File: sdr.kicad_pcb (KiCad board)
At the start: 4 copper layers, 65 x 56 mm, 224 parts, among them J1 RX, J2 TX, SW1 KMR231NGLFS, T1 B0322J5050, T2 B0322J5050, T3 TR_TC1-1-43X+, T4 TR_TC1-1-43X+, U1 FT601, U10 MIC94310, U11 PAM2305, U12 BGS12, U13 BGS12, U14 FT232HL, U15 93LCxxBT-I/OT, U3 LMS6002DR2, U4 ECP5, U5 Si5351, U6 PAM2305, U7 NCP186, U8 MIC94310, U9 MIC94310, X1 GSB443133HR, X2 JTAG, X3 RaspberryPiConnector, X4 JTAG, X5 USB_OTG, Y1 FL3000027, Y2 ABM11-141, Y3 ABLS2-12.000MHZ-D4Y-T

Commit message: Fix shield lines again.
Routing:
- net GNDD: track 839.6 -> 844.2 mm
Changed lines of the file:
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@@
 (kicad_pcb (version 4) (host pcbnew 4.0.6-e0-6349~53~ubuntu14.04.1)
   (general
-    (links 0)
+    (links 822)
     (no_connects 0)
-    (area 83.616521 95.152522 181.005759 157.677001)
+    (area 99.924999 99.924999 165.075001 156.075001)
     (thickness 1.6)
     (drawings 25)
-    (tracks 3914)
+    (tracks 3918)
     (zones 0)
     (modules 224)
@@
   )
   (setup
-    (last_trace_width 0.127)
+    (last_trace_width 0.762)
     (user_trace_width 0.2032)
     (user_trace_width 0.254)
@@
     (visible_elements FFFFFF79)
     (pcbplotparams
-      (layerselection 0x000fc_80000007)
-      (usegerberextensions false)
-      (excludeedgelayer false)
+      (layerselection 0x010fc_80000007)
+      (usegerberextensions true)
+      (excludeedgelayer true)
       (linewidth 0.100000)
       (plotframeref false)
@@
   (gr_line (start 158.1 106.4) (end 158.1 111.4) (angle 90) (layer F.CrtYd) (width 0.2))
   (segment (start 158.508601 127.108601) (end 158.3 126.9) (width 0.2032) (layer B.Cu) (net 0))
-  (segment (start 157.2709 135.4709) (end 157.47238 135.67238) (width 0.762) (layer B.Cu) (net 3))
-  (segment (start 157.47238 135.67238) (end 157.47238 137.5664) (width 0.762) (layer B.Cu) (net 3))
-  (segment (start 155.33116 135.4709) (end 157.2709 135.4709) (width 0.762) (layer B.Cu) (net 3))
+  (segment (start 157.47238 135.65886) (end 157.30982 135.4963) (width 0.762) (layer B.Cu) (net 3))
+  (segment (start 157.30982 135.4963) (end 155.7528 135.4963) (width 0.762) (layer B.Cu) (net 3))
+  (segment (start 157.47238 150.42262) (end 157.47238 135.65886) (width 0.762) (layer B.Cu) (net 3))
+  (segment (start 155.7528 135.4963) (end 149.0754 135.4963) (width 0.762) (layer F.Cu) (net 3))
+  (segment (start 149.0754 135.4963) (end 149.05 135.4709) (width 0.762) (layer F.Cu) (net 3))
+  (segment (start 157.46984 135.66648) (end 157.29966 135.4963) (width 0.762) (layer F.Cu) (net 3))
+  (segment (start 157.29966 135.4963) (end 155.7528 135.4963) (width 0.762) (layer F.Cu) (net 3))
+  (segment (start 157.46984 137.62736) (end 157.46984 135.66648) (width 0.762) (layer F.Cu) (net 3))
+  (segment (start 157.47238 140.48232) (end 157.47238 137.6299) (width 0.762) (layer F.Cu) (net 3))
+  (segment (start 157.47238 137.6299) (end 157.46984 137.62736) (width 0.762) (layer F.Cu) (net 3))
+  (via (at 155.7528 135.4963) (size 0.6858) (drill 0.381) (layers F.Cu B.Cu) (net 3))
+  (via (at 157.46984 137.62736) (size 0.6858) (drill 0.381) (layers F.Cu B.Cu) (net 3))
+  (segment (start 149.05 135.4709) (end 142.24762 135.4709) (width 0.762) (layer F.Cu) (net 3))
+  (segment (start 148.14296 135.4709) (end 147.5613 134.88924) (width 0.762) (layer B.Cu) (net 3))
   (segment (start 107.67568 130.83654) (end 103.26764 130.83654) (width 0.762) (layer F.Cu) (net 3))
   (segment (start 103.26764 130.83654) (end 102.5525 131.55168) (width 0.762) (layer F.Cu) (net 3))
@@
   (segment (start 150.41372 134.72444) (end 149.66726 135.4709) (width 0.254) (layer B.Cu) (net 3))
   (segment (start 149.66726 135.4709) (end 149.05 135.4709) (width 0.254) (layer B.Cu) (net 3))
-  (segment (start 147.96262 135.4709) (end 149.05 135.4709) (width 0.762) (layer F.Cu) (net 3))
-  (segment (start 149.05 135.4709) (end 155.33116 135.4709) (width 0.762) (layer F.Cu) (net 3))
   (segment (start 147.33548 134.08246) (end 148.72392 135.4709) (width 0.254) (layer B.Cu) (net 3))
   (segment (start 148.72392 135.4709) (end 149.05 135.4709) (width 0.254) (layer B.Cu) (net 3))
   (via (at 149.05 135.4709) (size 0.6858) (drill 0.381) (layers F.Cu B.Cu) (net 3))
-  (segment (start 147.96262 135.4709) (end 142.24762 135.4709) (width 0.762) (layer F.Cu) (net 3))
   (segment (start 147.98548 133.32846) (end 148.89866 133.32846) (width 0.254) (layer B.Cu) (net 3))
   (segment (start 148.89866 133.32846) (end 149.12086 133.55066) (width 0.254) (layer B.Cu) (net 3))
@@
   (segment (start 155.93 129.77682) (end 155.32608 130.38074) (width 0.127) (layer B.Cu) (net 3))
   (via (at 155.32608 130.38074) (size 0.6858) (drill 0.381) (layers F.Cu B.Cu) (net 3))
-  (segment (start 157.47238 150.42262) (end 157.47238 137.5664) (width 0.762) (layer B.Cu) (net 3))
   (segment (start 156.5529 153.9541) (end 156.5529 151.3421) (width 0.762) (layer B.Cu) (net 3))
   (segment (start 156.5529 151.3421) (end 157.47238 150.42262) (width 0.762) (layer B.Cu) (net 3))
-  (via (at 155.33116 135.4709) (size 0.6858) (drill 0.381) (layers F.Cu B.Cu) (net 3))
   (segment (start 157.47238 146.04238) (end 157.47238 150.42262) (width 0.762) (layer F.Cu) (net 3))
   (via (at 157.47238 150.42262) (size 0.6858) (drill 0.381) (layers F.Cu B.Cu) (net 3))
@@
   (via (at 157.47238 143.40078) (size 0.6858) (drill 0.381) (layers F.Cu B.Cu) (net 3))
   (via (at 157.47238 140.48232) (size 0.6858) (drill 0.381) (layers F.Cu B.Cu) (net 3))
-  (segment (start 157.47238 137.5664) (end 157.47238 140.48232) (width 0.762) (layer F.Cu) (net 3))
-  (via (at 157.47238 137.5664) (size 0.6858) (drill 0.381) (layers F.Cu B.Cu) (net 3))
   (segment (start 156.5529 153.9541) (end 156.5529 151.3421) (width 0.762) (layer F.Cu) (net 3))
   (segment (start 156.5529 151.3421) (end 157.47238 150.42262) (width 0.762) (layer F.Cu) (net 3))

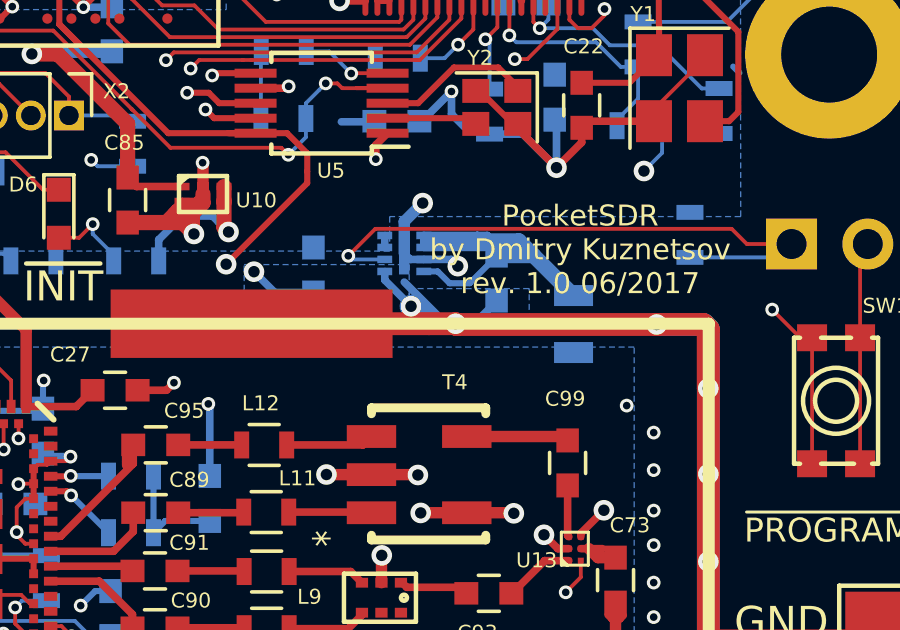
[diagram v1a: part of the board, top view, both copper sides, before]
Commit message: Start fixing problems with mask size and copper zone clearance.
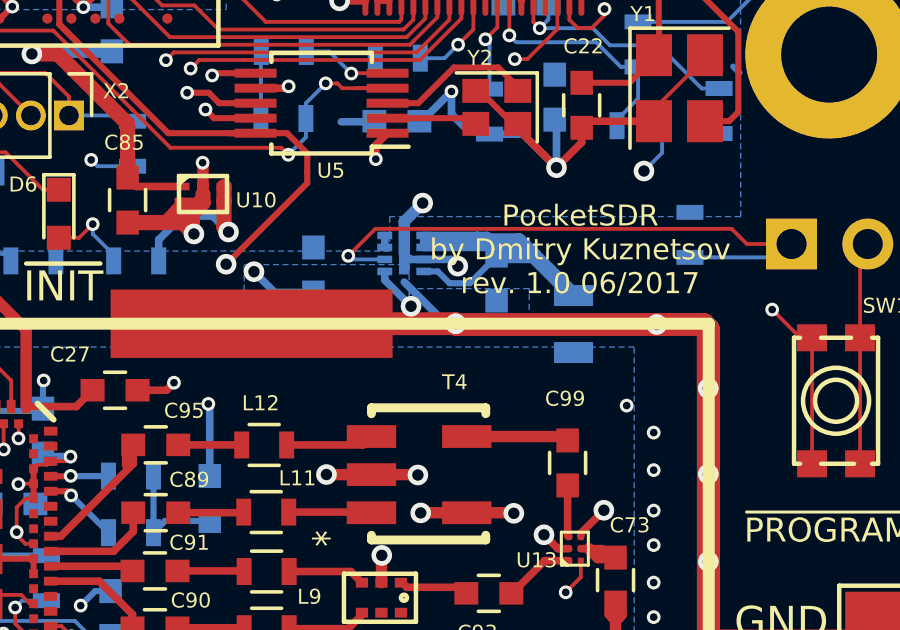
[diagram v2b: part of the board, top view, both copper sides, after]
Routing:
- net GNDD: track 844.2 -> 842.3 mm
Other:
- rule pad_to_mask_clearance: 0.2 -> 0.07112
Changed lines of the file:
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@@
-(kicad_pcb (version 4) (host pcbnew 4.0.6-e0-6349~53~ubuntu14.04.1)
+(kicad_pcb (version 4) (host pcbnew 4.0.7-e0-6372~58~ubuntu16.04.1)
   (general
     (links 822)
-    (no_connects 0)
-    (area 99.924999 99.924999 165.075001 156.075001)
+    (no_connects 6)
+    (area 83.616521 95.152522 181.005759 157.677001)
     (thickness 1.6)
     (drawings 25)
-    (tracks 3918)
+    (tracks 3916)
     (zones 0)
     (modules 224)
@@
   (title_block
     (title PocketSDR)
-    (date 2017-06-19)
-    (rev 1.0)
+    (date 2017-07-21)
+    (rev 1.1)
   )
   (layers
-    (0 F.Cu signal)
+    (0 F.Cu signal hide)
     (1 In1.Cu power hide)
-    (2 In2.Cu signal)
+    (2 In2.Cu signal hide)
     (31 B.Cu signal)
     (32 B.Adhes user hide)
@@
     (35 F.Paste user hide)
     (36 B.SilkS user)
-    (37 F.SilkS user)
-    (38 B.Mask user hide)
+    (37 F.SilkS user hide)
+    (38 B.Mask user)
     (39 F.Mask user hide)
     (40 Dwgs.User user hide)
@@
   )
   (setup
-    (last_trace_width 0.762)
+    (last_trace_width 0.127)
     (user_trace_width 0.2032)
     (user_trace_width 0.254)
@@
     (user_trace_width 0.762)
     (trace_clearance 0.127)
-    (zone_clearance 0.127)
+    (zone_clearance 0.254)
     (zone_45_only no)
     (trace_min 0.127)
@@
     (pad_size 0.29718 0.29718)
     (pad_drill 0)
-    (pad_to_mask_clearance 0.2)
+    (pad_to_mask_clearance 0.07112)
+    (solder_mask_min_width 0.127)
     (aux_axis_origin 124.58 122.04)
     (visible_elements FFFFFF79)
     (pcbplotparams
-      (layerselection 0x010fc_80000007)
-      (usegerberextensions true)
-      (excludeedgelayer true)
+      (layerselection 0x01010_00000000)
+      (usegerberextensions false)
+      (excludeedgelayer false)
       (linewidth 0.100000)
       (plotframeref false)
@@
       (plotvalue false)
       (plotinvisibletext false)
-      (padsonsilk false)
+      (padsonsilk true)
       (subtractmaskfromsilk false)
-      (outputformat 1)
-      (mirror false)
+      (outputformat 5)
+      (mirror true)
       (drillshape 0)
       (scaleselection 1)
@@
   (via (at 157.46984 137.62736) (size 0.6858) (drill 0.381) (layers F.Cu B.Cu) (net 3))
   (segment (start 149.05 135.4709) (end 142.24762 135.4709) (width 0.762) (layer F.Cu) (net 3))
-  (segment (start 148.14296 135.4709) (end 147.5613 134.88924) (width 0.762) (layer B.Cu) (net 3))
   (segment (start 107.67568 130.83654) (end 103.26764 130.83654) (width 0.762) (layer F.Cu) (net 3))
   (segment (start 103.26764 130.83654) (end 102.5525 131.55168) (width 0.762) (layer F.Cu) (net 3))
@@
   (via (at 142.32636 133.73608) (size 0.6858) (drill 0.381) (layers F.Cu B.Cu) (net 3))
   (segment (start 150.41372 134.69944) (end 150.41372 134.72444) (width 0.254) (layer B.Cu) (net 3))
-  (segment (start 150.41372 134.72444) (end 149.66726 135.4709) (width 0.254) (layer B.Cu) (net 3))
   (segment (start 149.66726 135.4709) (end 149.05 135.4709) (width 0.254) (layer B.Cu) (net 3))
   (segment (start 147.33548 134.08246) (end 148.72392 135.4709) (width 0.254) (layer B.Cu) (net 3))
@@
   (via (at 143.29 120.18) (size 0.6858) (drill 0.381) (layers F.Cu B.Cu) (net 286))
   (segment (start 152.94 123.4) (end 152.09 122.55) (width 0.2032) (layer B.Cu) (net 286))
-  (via (at 145.86 116.57) (size 0.4572) (drill 0.254) (layers F.Cu B.Cu) (net 286))
+  (via (at 145.86 116.57) (size 0.4572) (drill 0.254) (layers F.Cu B.Cu) (net 286) (status 1000000))
   (segment (start 152.47 115.28) (end 154.23 115.28) (width 0.2032) (layer B.Cu) (net 286))
   (segment (start 154.23 115.28) (end 154.7 115.75) (width 0.2032) (layer B.Cu) (net 286))
@@
   )
   (zone (net 286) (net_name VCCIO_FT) (layer B.Cu) (hatch none 0.508)
-    (connect_pads (clearance 0.127))
-    (min_thickness 0.127)
-    (fill yes (arc_segments 16) (thermal_gap 0.127) (thermal_bridge_width 0.2032) (smoothing fillet) (radius 0.508))
+    (connect_pads (clearance 0.254))
+    (min_thickness 0.254)
+    (fill yes (arc_segments 16) (thermal_gap 0.254) (thermal_bridge_width 0.2794) (smoothing fillet) (radius 0.508))
     (polygon
       (pts
@@
   )
   (zone (net 61) (net_name LMS_A3V3) (layer B.Cu) (hatch edge 0.508)
-    (connect_pads (clearance 0.127))
-    (min_thickness 0.125)
-    (fill yes (arc_segments 16) (thermal_gap 0.254) (thermal_bridge_width 0.254) (smoothing fillet) (radius 0.508))
+    (connect_pads (clearance 0.254))
+    (min_thickness 0.254)
+    (fill yes (arc_segments 16) (thermal_gap 0.254) (thermal_bridge_width 0.2794) (smoothing fillet) (radius 0.508))
     (polygon
       (pts

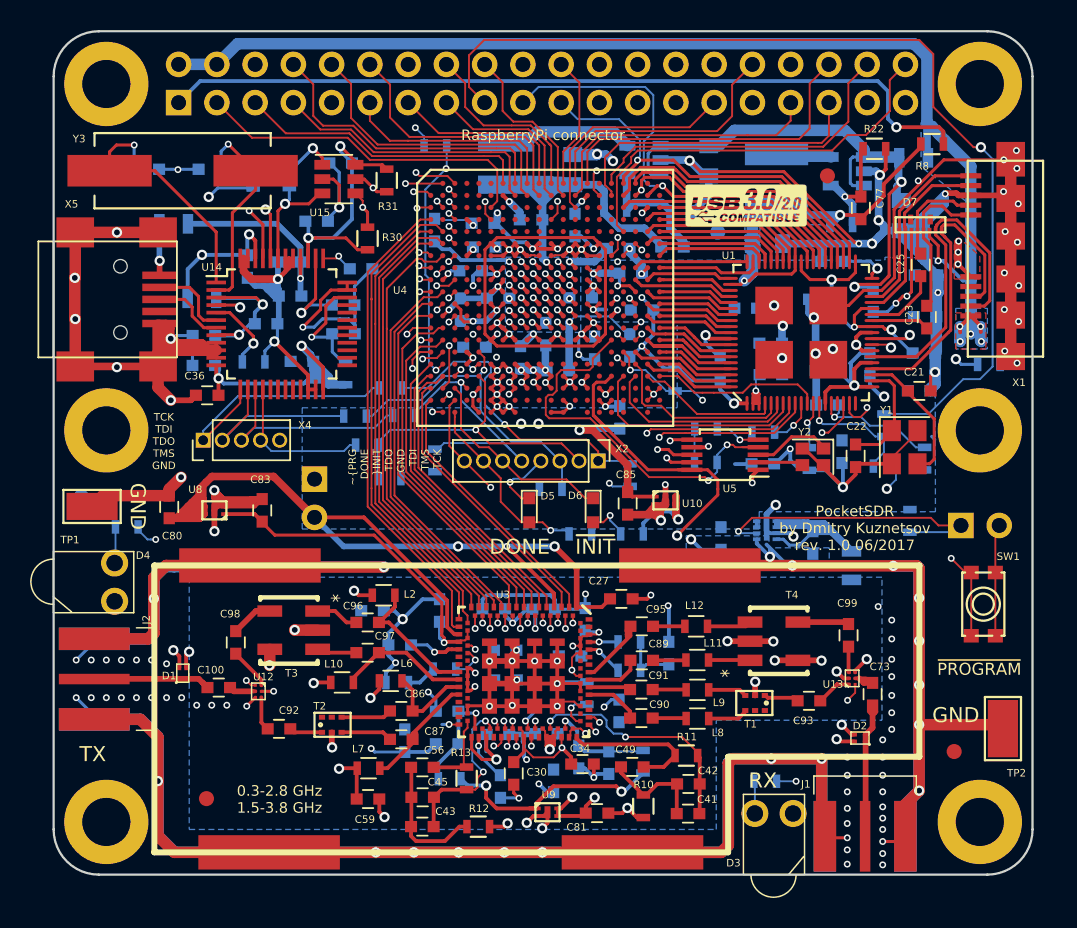
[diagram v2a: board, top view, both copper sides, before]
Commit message: Finish fixing problems: 1. LDO 3V3A has been changed as well as it CAPs 2. Silkscreen fixed 3. Mask expansion is changed
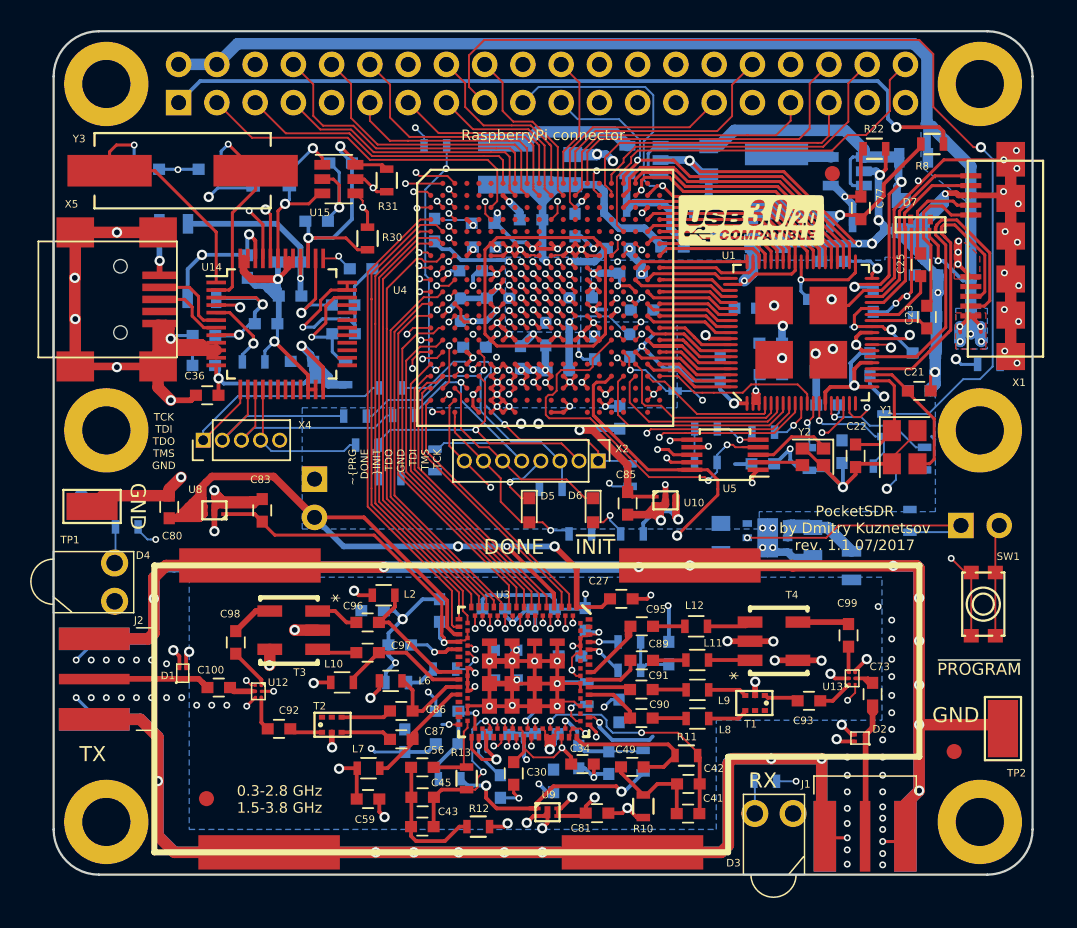
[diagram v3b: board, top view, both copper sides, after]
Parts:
- C78, C79: value 1u -> 10u; footprint Capacitors_SMD:C_0603 -> Capacitors_SMD:C_0805
- U7: value NCP186 -> LD39200; footprint sdr-foots:DFN-8-1EP_1.6x1.2mm_Pitch0.4mm -> Housings_DFN_QFN:DFN-6-1EP_3x3mm_Pitch0.95mm
- moved G*** 1.05 mm to (146.3, 112.6)
- moved U7 0.51 mm to (147.4, 133.6)
- moved REF** 0.36 mm to (151.7, 109.4)
- turned C1 to 0 degrees
- turned C7 to 180 degrees
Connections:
- U7 pad 4: Net-(C79-Pad1) -> Net-(U7-Pad4)
- U7 pad 5: GNDD -> Net-(JP1-Pad1)
- U7 pad 6: Net-(JP1-Pad1) -> VCCIO_FT
- U7 pad 7: VCCIO_FT -> GNDD
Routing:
- net GNDD: track 842.3 -> 852.5 mm, vias 231 -> 232
- net Net-(C79-Pad1): track 16.8 -> 7.65 mm
- net LMS_A3V3: track 38.9 -> 44.5 mm
- net VCCIO_FT: track 136.7 -> 133.0 mm
- net Net-(JP1-Pad1): track 20.2 -> 18.1 mm
- net /Power/DV10: track 20.4 -> 18.6 mm
- net CLK0: track 44.2 -> 45.8 mm
- removed copper zone on B.Cu, net GNDD
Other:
- board text added: "PocketSDR by Dmitry Kuznetsov rev. 1.1 07/2017"
- board text removed: "PocketSDR by Dmitry Kuznetsov rev. 1.0 06/2017"
